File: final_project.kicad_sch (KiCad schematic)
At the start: 3 parts, among them J1 USB4110GFA, U1 STM32L476RCTx, U2 USBLC6-2SC6

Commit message: This should be the most recent one
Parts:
- removed J1: USB4110GFA, USB4110GFA:GCT_USB4110GFA, symbol USB4110GFA:USB4110GFA
- removed U1: STM32L476RCTx, Package_QFP:LQFP-64_10x10mm_P0.5mm, symbol MCU_ST_STM32L4:STM32L476RCTx
- removed U2: USBLC6-2SC6, USBLC6-2SC6:SOT95P280X145-6N, symbol USBLC6-2SC6:USBLC6-2SC6
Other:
- removed sheet Microcontroller connections
- added sheet MCU (MCU.kicad_sch)
- added sheet USB (USB.kicad_sch)

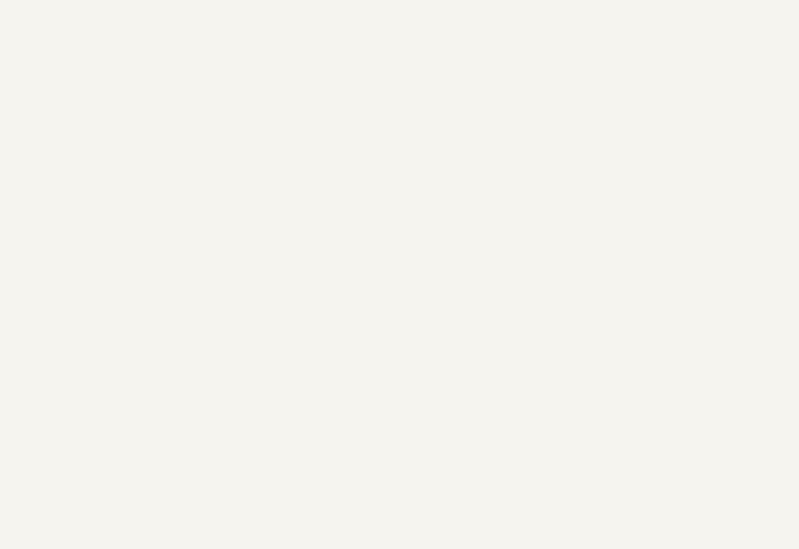
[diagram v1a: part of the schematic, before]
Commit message: added power switch and RF module
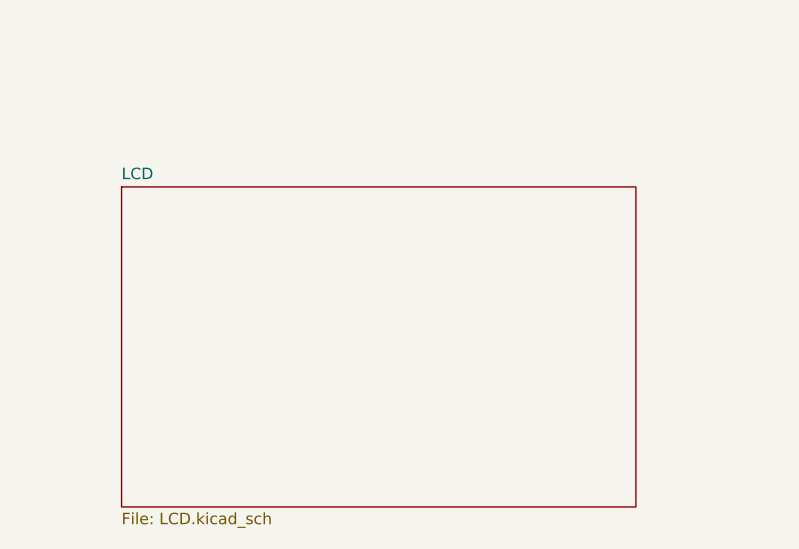
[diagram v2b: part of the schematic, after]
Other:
- added sheet LCD (LCD.kicad_sch)
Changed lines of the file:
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@@
+		)
+	)
+	(sheet
+		(at 38.1 113.03)
+		(size 57.15 35.56)
+		(exclude_from_sim no)
+		(in_bom yes)
+		(on_board yes)
+		(dnp no)
+		(fields_autoplaced yes)
+		(stroke
+			(width 0.1524)
+			(type solid)
+		)
+		(fill
+			(color 0 0 0 0.0000)
+		)
+		(property "Sheetname" "LCD"
+			(at 38.1 112.3184 0)
+			(effects
+				(font
+					(size 1.27 1.27)
+				)
+				(justify left bottom)
+			)
+		)
+		(property "Sheetfile" "LCD.kicad_sch"
+			(at 38.1 149.1746 0)
+			(effects
+				(font
+					(size 1.27 1.27)
+				)
+				(justify left top)
+			)
+		)
+		(instances
+			(project "final_project"
+				(path "/bcf3418e-986f-42d9-beb5-94c6e2a384e4"
+					(page "4")
+				)
+			)
 		)
 	)
